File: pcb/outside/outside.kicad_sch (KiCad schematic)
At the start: 56 parts, among them J1 USB_C_Receptacle_USB2.0_16P, J2 RJ12, J3 Conn_01x08, J4 Conn_01x04, Q1 NMOS, SW1 RST, SW2 PRG, U1 ESP32-C6-MINI-1, U2 MFRC52201HN1,157, U3 USBLC6-2P6, U4 AMS1117-3.3, Y1 XRCGB27M120F3M13R0

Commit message: fix: add part number
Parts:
- LS1: value Speaker_Crystal -> PS1240P02BT
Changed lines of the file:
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@@
 			)
 		)
-		(property "Value" "Speaker_Crystal"
+		(property "Value" "PS1240P02BT"
 			(at 139.7 118.1099 0)
 			(effects
@@
 			)
 		)
-		(property "Datasheet" "~"
+		(property "Datasheet" "https://product.tdk.com/system/files/dam/doc/product/sw_piezo/sw_piezo/piezo-buzzer/catalog/piezoelectronic_buzzer_ps_en.pdf"
 			(at 133.731 116.84 0)
 			(effects

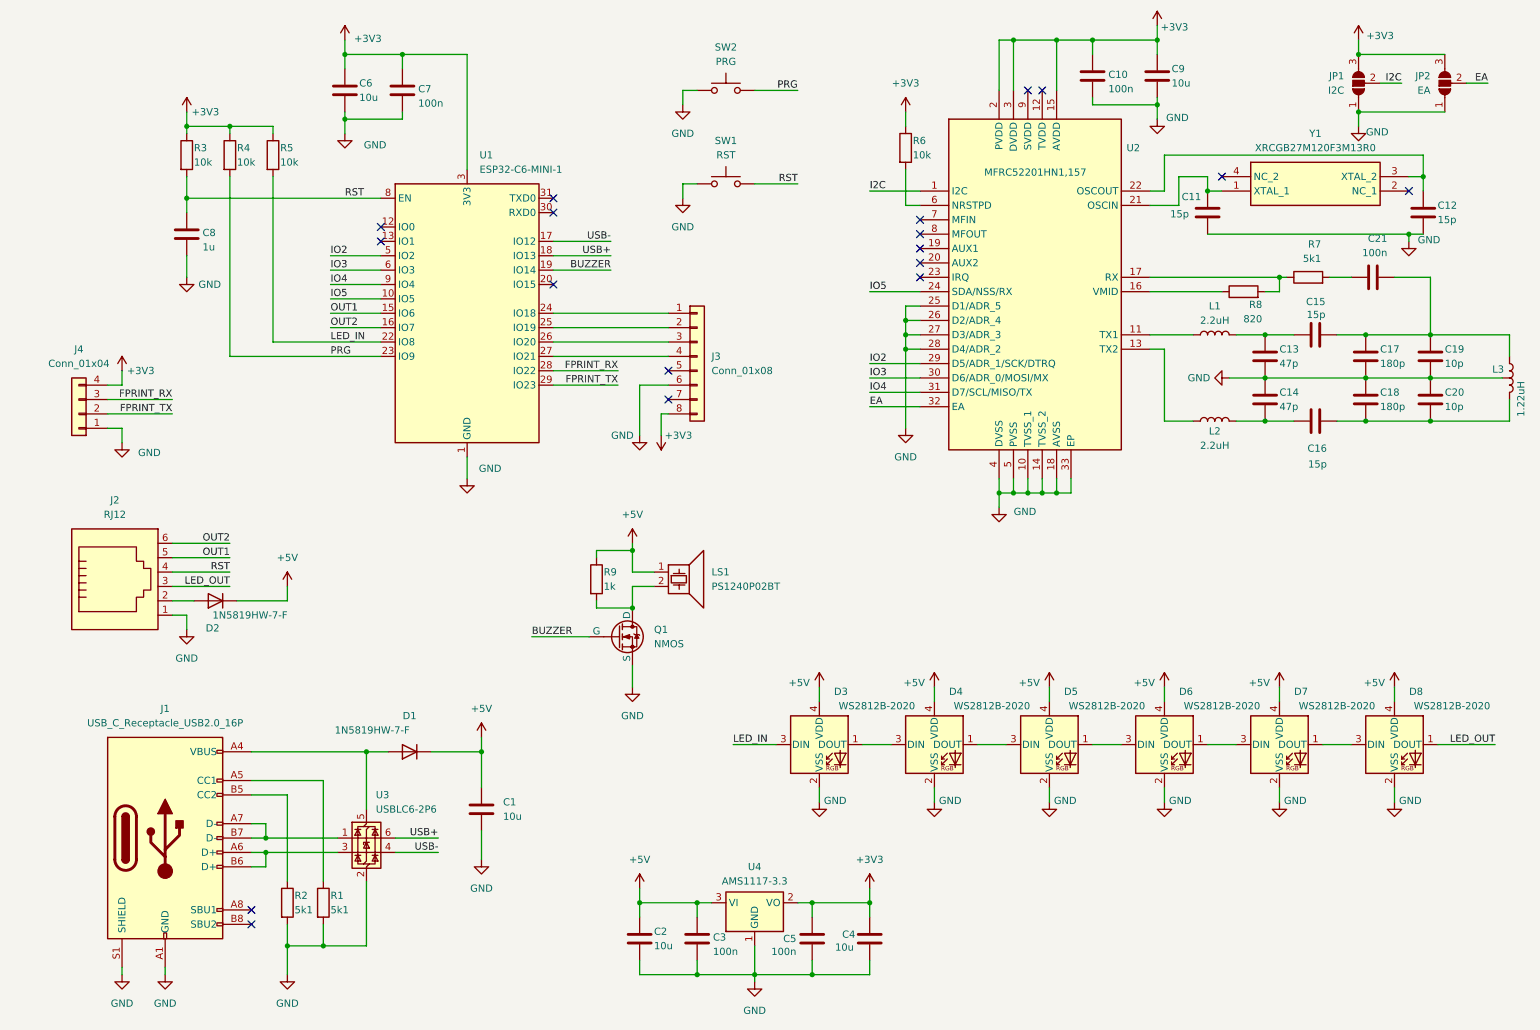
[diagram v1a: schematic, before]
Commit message: feat: improve and rearrange schematic
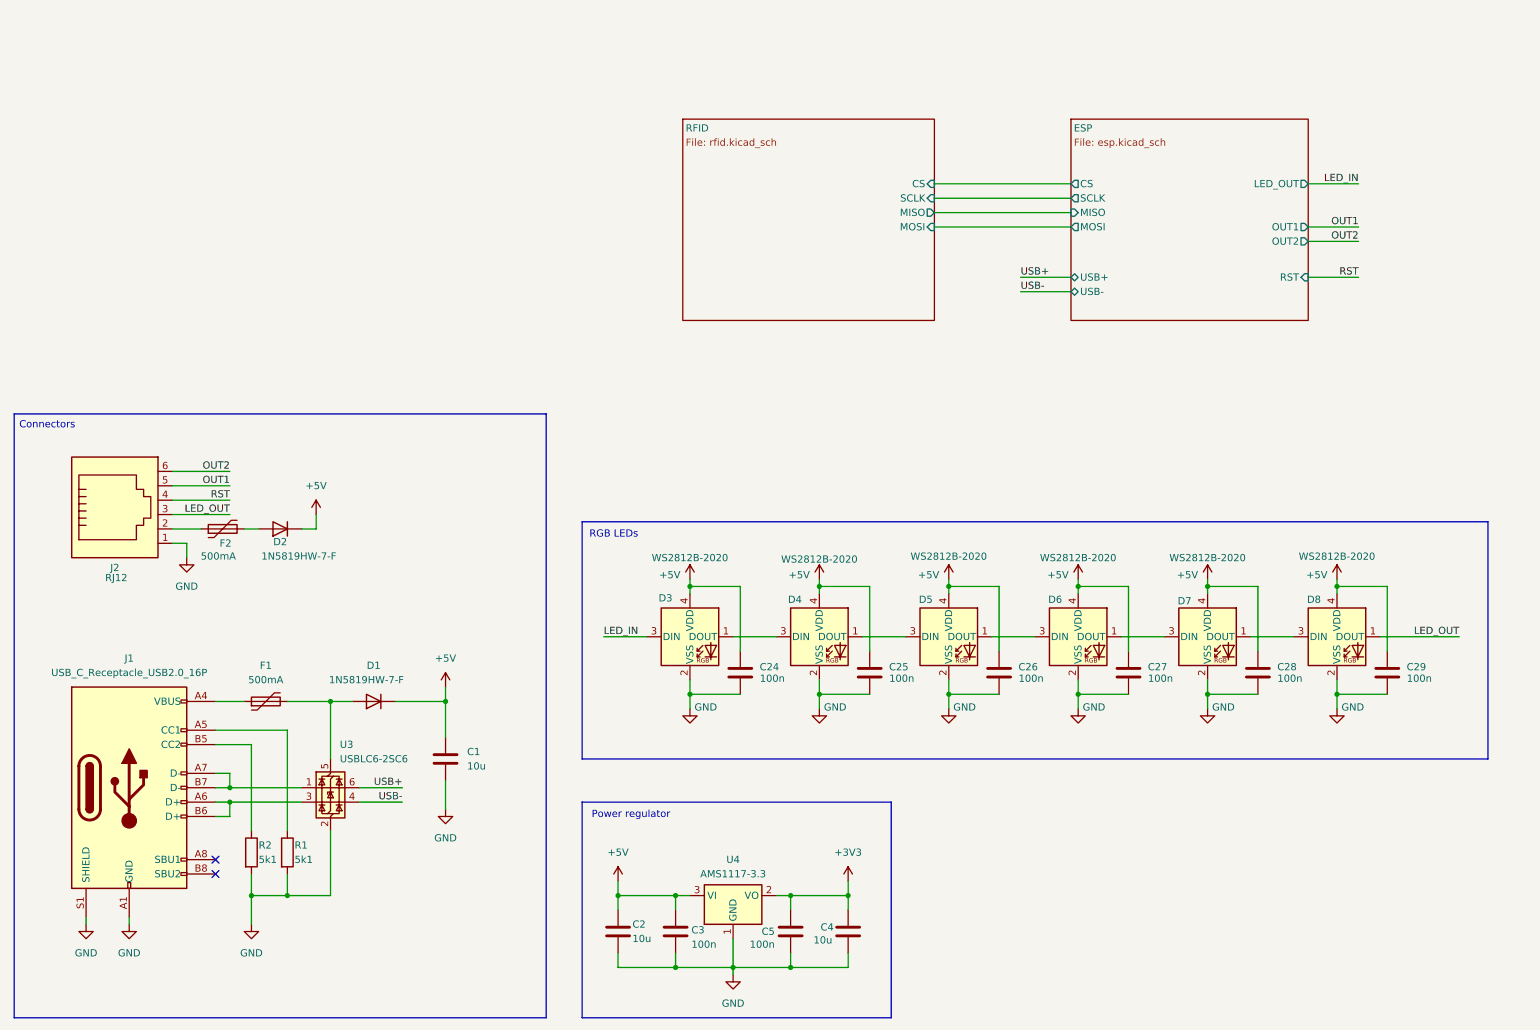
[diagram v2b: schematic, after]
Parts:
- removed C10, C21, C7: 100n, Capacitor_SMD:C_0603_1608Metric, symbol Device:C
- removed C11, C12, C15, C16: 15p, Capacitor_SMD:C_0603_1608Metric, symbol Device:C
- removed C13, C14: 47p, Capacitor_SMD:C_0603_1608Metric, symbol Device:C
- removed C17, C18: 180p, Capacitor_SMD:C_0603_1608Metric, symbol Device:C
- removed C19, C20: 10p, Capacitor_SMD:C_0603_1608Metric, symbol Device:C
- removed C6, C9: 10u, Capacitor_SMD:C_0603_1608Metric, symbol Device:C
- removed C8: 1u, Capacitor_SMD:C_0603_1608Metric, symbol Device:C
- removed J3: Conn_01x08, Connector_PinSocket_2.54mm:PinSocket_1x08_P2.54mm_Vertical, symbol Connector_Generic:Conn_01x08
- removed J4: Conn_01x04, Connector_JST:JST_XH_B4B-XH-A_1x04_P2.50mm_Vertical, symbol Connector_Generic:Conn_01x04
- removed JP1: I2C, Jumper:SolderJumper-3_P1.3mm_Open_RoundedPad1.0x1.5mm, symbol Jumper:SolderJumper_3_Open
- removed JP2: EA, Jumper:SolderJumper-3_P1.3mm_Open_RoundedPad1.0x1.5mm, symbol Jumper:SolderJumper_3_Open
- removed L1, L2: 2.2uH, Inductor_SMD:L_0603_1608Metric, symbol Device:L
- removed L3: 1.22uH, belepteto:RFID_PCB_ant, symbol belepteto:RFID_PCB_ant
- removed LS1: PS1240P02BT, belepteto:PS1240P02BT, symbol Device:Speaker_Crystal
- removed Q1: NMOS, Package_TO_SOT_SMD:SOT-23, symbol Simulation_SPICE:NMOS
- removed R3, R4, R5, R6: 10k, Resistor_SMD:R_0603_1608Metric, symbol Device:R
- removed R7: 5k1, Resistor_SMD:R_0603_1608Metric, symbol Device:R
- removed R8: 820, Resistor_SMD:R_0603_1608Metric, symbol Device:R
- removed R9: 1k, Resistor_SMD:R_0603_1608Metric, symbol Device:R
- removed SW1: RST, Button_Switch_SMD:SW_SPST_CK_RS282G05A3, symbol Switch:SW_Push
- removed SW2: PRG, Button_Switch_SMD:SW_SPST_CK_RS282G05A3, symbol Switch:SW_Push
- removed U1: ESP32-C6-MINI-1, RF_Module:ESP32-C6-MINI-1, symbol RF_Module:ESP32-C6-MINI-1
- removed U2: MFRC52201HN1,157, Package_DFN_QFN:QFN-32-1EP_5x5mm_P0.5mm_EP3.1x3.1mm, symbol belepteto:MFRC52201HN1,157
- removed U3: USBLC6-2P6, Package_TO_SOT_SMD:SOT-666, symbol Power_Protection:USBLC6-2P6
- removed Y1: XRCGB27M120F3M13R0, belepteto:XRCGB, symbol belepteto:XRCGB27M120F3M13R0
- added C24, C25, C26, C27, C28, C29: 100n, Capacitor_SMD:C_0603_1608Metric, symbol Device:C
- added F1, F2: 500mA, belepteto:1206L05015YR, symbol Device:Polyfuse
- added U3: USBLC6-2SC6, Package_TO_SOT_SMD:SOT-23-6, symbol Power_Protection:USBLC6-2SC6
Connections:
- net +5V: now also C24.2, C25.2, C26.2, C27.2, C28.2, C29.2
- net GND: now also C24.1, C25.1, C26.1, C27.1, C28.1, C29.1, U3.2 (GND)
- net USB+: now also U3.6 (I/O1)
- net USB-: now also U3.4 (I/O2)
- net at J1.A4 (VBUS), J1.A9 (VBUS), J1.B4 (VBUS)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: now also F1.1; no longer D1.2 (A)
- net at J1.A6 (D+), J1.B6 (D+): now also U3.3 (I/O2)
- net at J1.A7 (D-), J1.B7 (D-): now also U3.1 (I/O1)
- net at J2.2: now also F2.1; no longer D2.2 (A)
- new net: D2.2 (A), F2.2
- new net: D1.2 (A), F1.2, U3.5 (VBUS)
- no-connect marks 18 -> 2
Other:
- added sheet ESP (esp.kicad_sch)
- added sheet RFID (rfid.kicad_sch)
- note added: "Connectors"
- note added: "Power regulator"
- note added: "RGB LEDs"
- moved on the sheet: C1, C2, C3, C4, C5, D1, D2, D3, D4, D5, D6, D7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

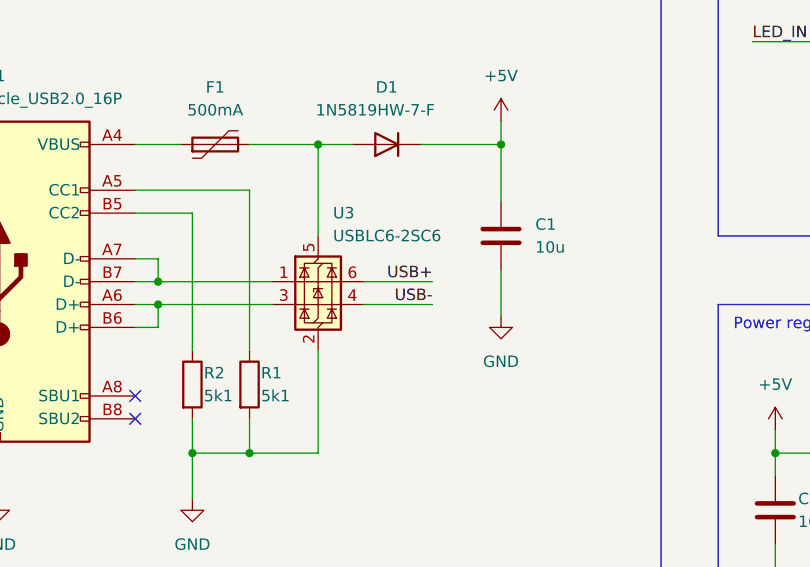
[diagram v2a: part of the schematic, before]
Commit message: fix: USB polarity
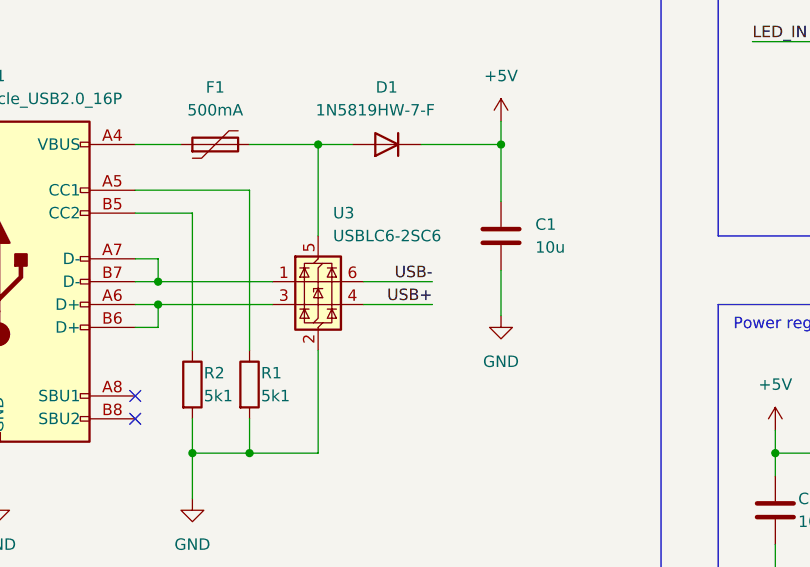
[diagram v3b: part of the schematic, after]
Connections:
- net USB+: now also U3.4 (I/O2); no longer U3.6 (I/O1)
- net USB-: now also U3.6 (I/O1); no longer U3.4 (I/O2)
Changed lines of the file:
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@@
 		)
 	)
-	(label "USB-"
+	(label "USB+"
 		(at 85.09 156.21 180)
 		(effects
@@
 		)
 	)
-	(label "USB+"
+	(label "USB-"
 		(at 85.09 153.67 180)
 		(effects

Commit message: feat: add testpoints and rearrange schematic
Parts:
- removed U3: USBLC6-2SC6, Package_TO_SOT_SMD:SOT-23-6, symbol Power_Protection:USBLC6-2SC6
- added C2, C3: 10u, Capacitor_SMD:C_0603_1608Metric, symbol Device:C
- added C4: 1u, Capacitor_SMD:C_0603_1608Metric, symbol Device:C
- added C5, C6: 100n, Capacitor_SMD:C_0603_1608Metric, symbol Device:C
- added J3: Conn_01x08, Connector_PinSocket_2.54mm:PinSocket_1x08_P2.54mm_Vertical, symbol Connector_Generic:Conn_01x08
- added J4: Conn_01x04, Connector_JST:JST_XH_B4B-XH-A_1x04_P2.50mm_Vertical, symbol Connector_Generic:Conn_01x04
- added LS1: PS1240P02BT, belepteto:PS1240P02BT, symbol Device:Speaker_Crystal
- added Q1: BSS138, Package_TO_SOT_SMD:SOT-23, symbol Transistor_FET:BSS138
- added R3, R4, R5: 10k, Resistor_SMD:R_0603_1608Metric, symbol Device:R
- added R6, R7: 5k1, Resistor_SMD:R_0603_1608Metric, symbol Device:R
- added R8, R9: 22, Resistor_SMD:R_0603_1608Metric, symbol Device:R
- added SW1: RST, Button_Switch_SMD:SW_SPST_TL3342, symbol Switch:SW_Push
- added SW2: PRG, Button_Switch_SMD:SW_SPST_TL3342, symbol Switch:SW_Push
- added TP1: BUZZER, TestPoint:TestPoint_Pad_D1.0mm, symbol Connector:TestPoint
- added TP10: OUT2, TestPoint:TestPoint_Pad_D1.0mm, symbol Connector:TestPoint
- added TP11: OUT1, TestPoint:TestPoint_Pad_D1.0mm, symbol Connector:TestPoint
- added TP12: EXT_MISO, TestPoint:TestPoint_Pad_D1.0mm, symbol Connector:TestPoint
- added TP13: EXT_MOSI, TestPoint:TestPoint_Pad_D1.0mm, symbol Connector:TestPoint
- added TP14: LED_IN, TestPoint:TestPoint_Pad_D1.0mm, symbol Connector:TestPoint
- added TP15: LED_OUT, TestPoint:TestPoint_Pad_D1.0mm, symbol Connector:TestPoint
- added TP16: EXT_SCLK, TestPoint:TestPoint_Pad_D1.0mm, symbol Connector:TestPoint
- added TP17: EXT_CS, TestPoint:TestPoint_Pad_D1.0mm, symbol Connector:TestPoint
- added TP18: FPRINT_RX, TestPoint:TestPoint_Pad_D1.0mm, symbol Connector:TestPoint
- added TP19: FPRINT_TX, TestPoint:TestPoint_Pad_D1.0mm, symbol Connector:TestPoint
- added TP2: ESP_RST, TestPoint:TestPoint_Pad_D1.0mm, symbol Connector:TestPoint
- added TP20: +5V, TestPoint:TestPoint_Pad_D1.0mm, symbol Connector:TestPoint
- added TP21: +3V3, TestPoint:TestPoint_Pad_D1.0mm, symbol Connector:TestPoint
- added TP22: GND, TestPoint:TestPoint_Pad_D1.0mm, symbol Connector:TestPoint
- added TP3: ESP_TX, TestPoint:TestPoint_Pad_D1.0mm, symbol Connector:TestPoint
- added TP4: ESP_RX, TestPoint:TestPoint_Pad_D1.0mm, symbol Connector:TestPoint
- added TP5: ESP_PRG, TestPoint:TestPoint_Pad_D1.0mm, symbol Connector:TestPoint
- added TP6: INT_CS, TestPoint:TestPoint_Pad_D1.0mm, symbol Connector:TestPoint
- added TP7: INT_SCLK, TestPoint:TestPoint_Pad_D1.0mm, symbol Connector:TestPoint
- added TP8: INT_MISO, TestPoint:TestPoint_Pad_D1.0mm, symbol Connector:TestPoint
- added TP9: INT_MOSI, TestPoint:TestPoint_Pad_D1.0mm, symbol Connector:TestPoint
- added U1: ESP32-C6-MINI-1, RF_Module:ESP32-C6-MINI-1, symbol RF_Module:ESP32-C6-MINI-1
- added U4, U5: USBLC6-2SC6, Package_TO_SOT_SMD:SOT-23-6, symbol Power_Protection:USBLC6-2SC6
- C1: value 10u -> 100n
- R1: value 5k1 -> 1k
- R2: value 5k1 -> 180
- renumbered C27 to C10, C28 to C11, C29 to C12, C2 to C13, C3 to C14, C5 to C15, C4 to C16, C24 to C7, C25 to C8, C26 to C9, U4 to U3
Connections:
- net +3V3: now also C1.1, C2.1, J3.8 (Pin_8), J4.4 (Pin_4), R3.1, R4.1, R5.1, TP21.1, U1.3 (3V3), U5.5 (VBUS)
- net +5V: now also R1.1, C3.1, LS1.1, TP20.1; no longer C1.1
- net GND: now also C2.2, C3.2, C4.2, C5.1, C6.1, J3.6 (Pin_6), J4.1 (Pin_1), Q1.2 (S), R6.2, R7.2, SW1.1, SW2.1, TP22.1, U1.1 (GND), U1.11 (GND), U1.14 (GND), U1.2 (GND), U1.36 (GND), U1.37 (GND), U1.38 (GND), U1.39 (GND), U1.40 (GND), U1.41 (GND), U1.42 (GND), U1.43 (GND), U1.44 (GND), U1.45 (GND), U1.46 (GND), U1.47 (GND), U1.48 (GND), U1.49 (GND), U1.50 (GND), U1.51 (GND), U1.52 (GND), U1.53 (GND), U4.2 (GND), U5.2 (GND); no longer R1.2, R2.2
- net LED_IN: now also R4.2, TP14.1, U1.22 (IO8)
- net LED_OUT: now also TP15.1
- net OUT1: now also TP11.1, U1.15 (IO6)
- net OUT2: now also TP10.1, U1.16 (IO7)
- net RST: now also C4.1, C5.2, R5.2, SW1.2, TP2.1, U1.8 (EN)
- net USB+: now also U1.18 (IO13), U4.4 (I/O2)
- net USB-: now also U1.17 (IO12), U4.6 (I/O1)
- net USB_CC1: now reaches J1.A5 (CC1)
- net USB_CC1: now also R7.1; no longer R1.1
- net BUZZER: now reaches R2.1
- net BUZZER: now also TP1.1, U1.19 (IO14); no longer J1.B5 (CC2)
- net USBC+: now reaches J1.A6 (D+), J1.B6 (D+)
- net USBC+: now also U4.3 (I/O2)
- net USBC-: now reaches J1.A7 (D-), J1.B7 (D-)
- net USBC-: now also U4.1 (I/O1)
- net at D1.2 (A), F1.2: now also U4.5 (VBUS)
- new net: R8.2, U5.1 (I/O1)
- new net: R9.2, U5.3 (I/O2)
- new net: TP3.1, U1.31 (TXD0)
- new net: J4.2 (Pin_2), R9.1
- new net: J4.3 (Pin_3), R8.1
- new net: TP4.1, U1.30 (RXD0)
- new net: Q1.1 (G), R2.2
- new net: LS1.2, Q1.3 (D), R1.2
- new net CS: TP6.1, U1.10 (IO5)
- new net EXT_CS: J3.1 (Pin_1), TP17.1, U1.24 (IO18)
- new net EXT_MISO: J3.4 (Pin_4), TP12.1, U1.27 (IO21)
- new net EXT_MOSI: J3.3 (Pin_3), TP13.1, U1.26 (IO20)
- new net EXT_SCLK: J3.2 (Pin_2), TP16.1, U1.25 (IO19)
- new net FPRINT_RX: TP18.1, U1.28 (IO22), U5.6 (I/O1)
- new net FPRINT_TX: TP19.1, U1.29 (IO23), U5.4 (I/O2)
- new net MISO: TP8.1, U1.9 (IO4)
- new net MOSI: TP9.1, U1.6 (IO3)
- new net PRG: C6.2, R3.2, SW2.2, TP5.1, U1.23 (IO9)
- new net SCLK: TP7.1, U1.5 (IO2)
- new net USB_CC2: J1.B5 (CC2), R6.1
- no-connect marks 2 -> 7
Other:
- removed sheet ESP
- note added: "Buzzer"
- note added: "ESP"
- note added: "External RC522"
- note added: "Fingerprint reader"
- note added: "For programming"
- note added: "To inside PCB"
- moved on the sheet: C10, C11, C12, C13, C14, C15, C16, C7, C8, C9, D3, D4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
